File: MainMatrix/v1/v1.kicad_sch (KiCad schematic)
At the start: 180 parts, among them J1 Conn_01x16, J2 Conn_01x06

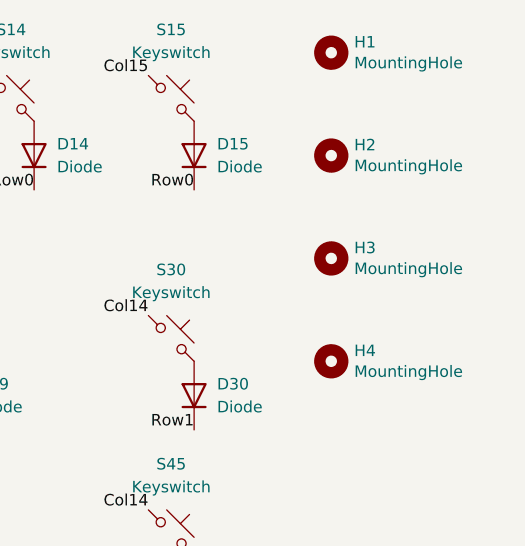
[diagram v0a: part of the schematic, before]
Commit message: Created Main Matrix v2 split.
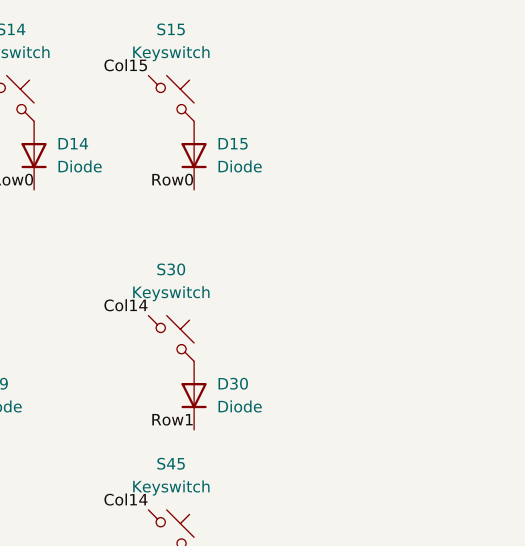
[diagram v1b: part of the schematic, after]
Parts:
- removed H1, H2, H3, H4: MountingHole, MountingHole:MountingHole_3.2mm_M3_DIN965, symbol Mechanical:MountingHole

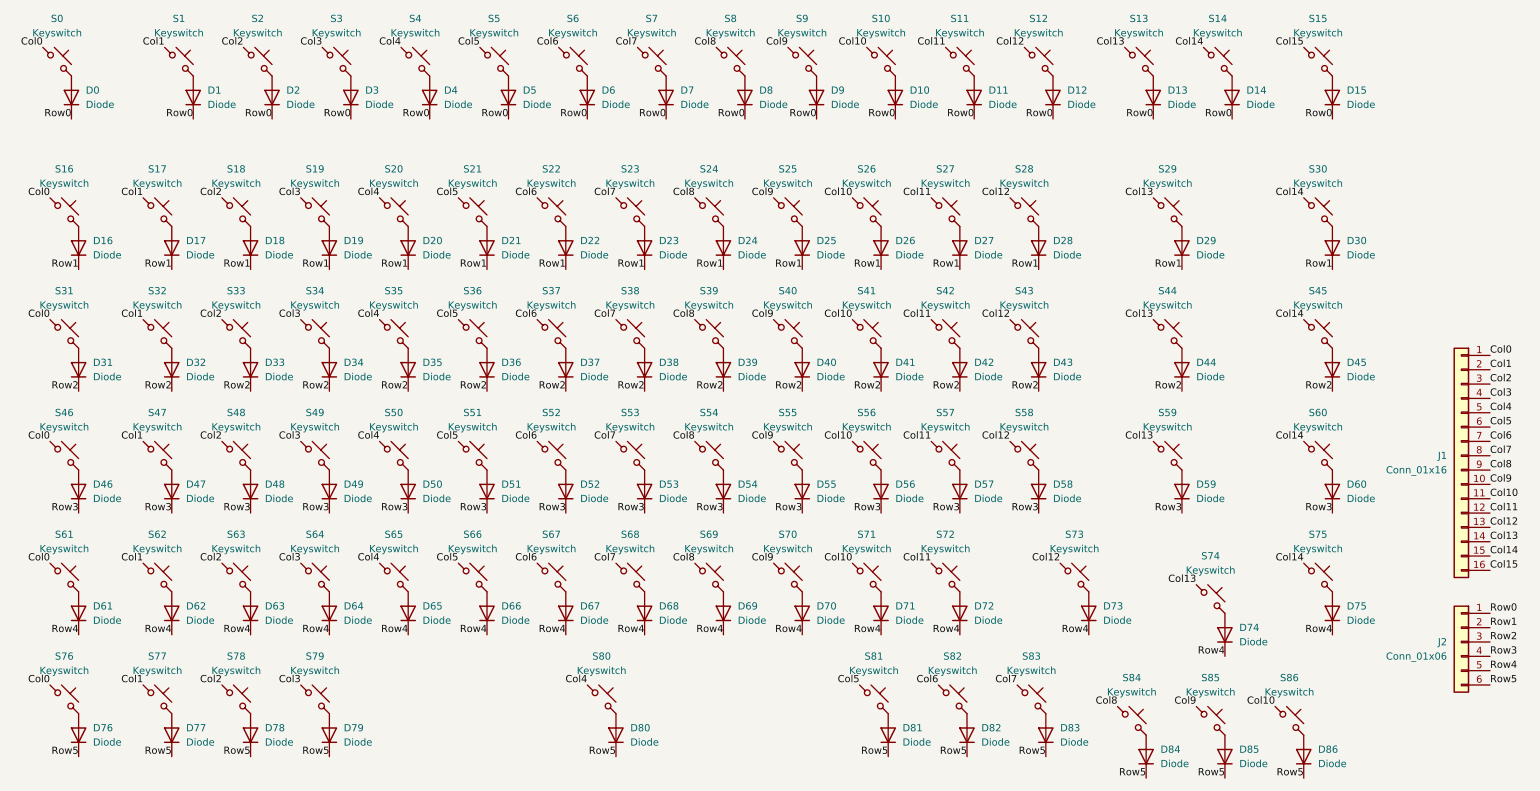
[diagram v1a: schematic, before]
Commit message: Improvements to the MainMatrix board~
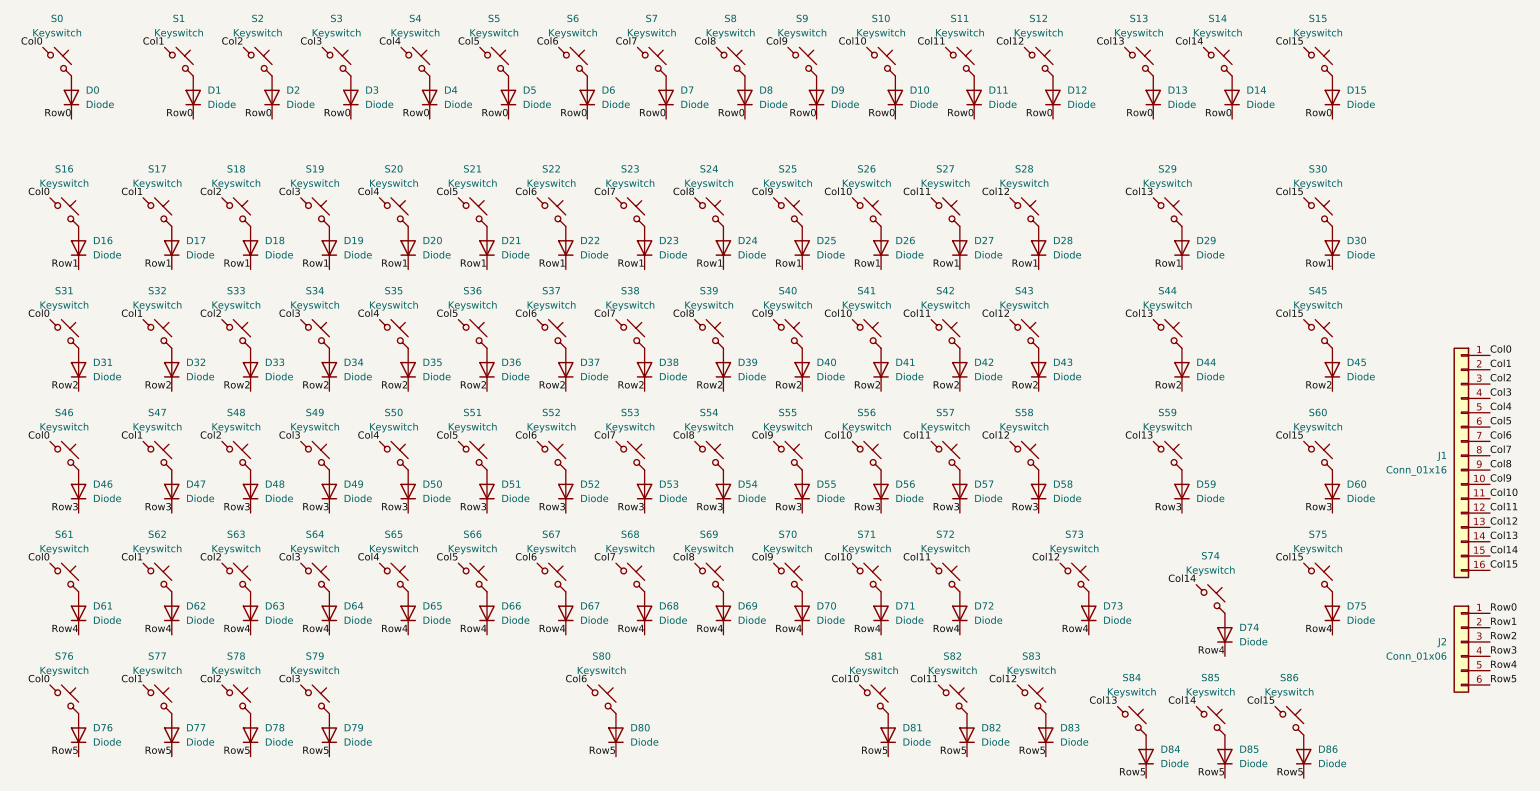
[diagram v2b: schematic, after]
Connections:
- net Col10: now also S81.1; no longer S86.1
- net Col11: now also S82.1
- net Col12: now also S83.1
- net Col13: now also S84.1; no longer S74.1
- net Col14: now also S74.1, S85.1; no longer S30.1, S45.1, S60.1, S75.1
- net Col15: now also S30.1, S45.1, S60.1, S75.1, S86.1
- net Col4: no longer S80.1
- net Col5: no longer S81.1
- net Col6: now also S80.1; no longer S82.1
- net Col7: no longer S83.1
- net Col8: no longer S84.1
- net Col9: no longer S85.1
